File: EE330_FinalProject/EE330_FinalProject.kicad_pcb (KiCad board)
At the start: 2 copper layers, 20 parts, among them IC1 LT1490AIS8#PBF, J1 01x04_Pin, Q1 2N3904, Q2 2N3904, Q3 2N3904, Q4 2N3904

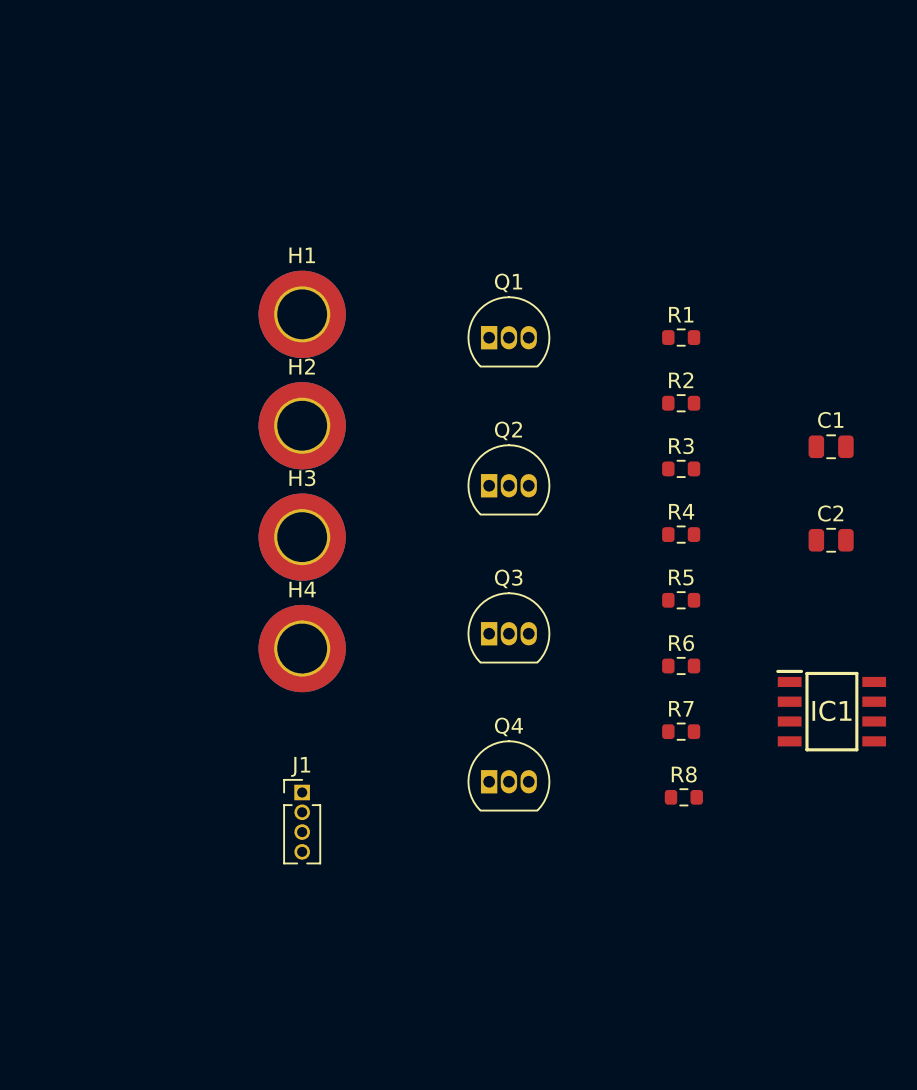
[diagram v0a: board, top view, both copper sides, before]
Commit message: Updated schematic and PCB based on the testing done today. Need to confirm physical setup before finalizing
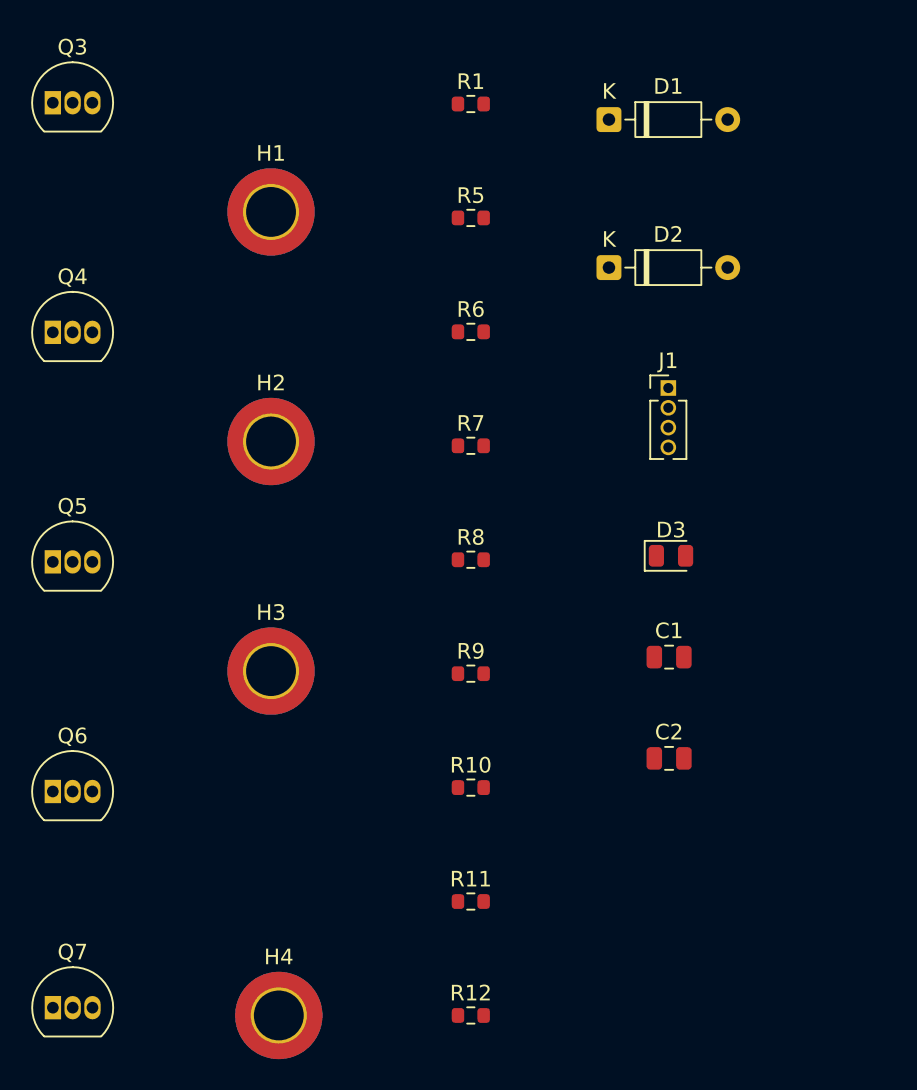
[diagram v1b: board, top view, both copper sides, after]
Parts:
- removed IC1: LT1490AIS8#PBF, Circuit_Craft_Footprints:LT1490
- removed Q1, Q2: 2N3904, Package_TO_SOT_THT:TO-92_Inline
- removed R2, R3, R4: 10k, Resistor_SMD:R_0603_1608Metric
- added D1: 1N4148, Diode_THT:D_DO-35_SOD27_P7.62mm_Horizontal, F.Cu at (65.2, 33.5)
- added D2: 1N4148, Diode_THT:D_DO-35_SOD27_P7.62mm_Horizontal, F.Cu at (65.2, 43.0)
- added D3: RED_LED, LED_SMD:LED_0805_2012Metric, F.Cu at (69.2, 61.5)
- added Q5: 2N3906, Package_TO_SOT_THT:TO-92_Inline, F.Cu at (29.5, 61.9)
- added Q6: 2N3904, Package_TO_SOT_THT:TO-92_Inline, F.Cu at (29.5, 76.6)
- added Q7: 2N3904, Package_TO_SOT_THT:TO-92_Inline, F.Cu at (29.5, 90.5)
- added R10: 1M, Resistor_SMD:R_0603_1608Metric, F.Cu at (56.3, 76.4)
- added R11: 1M, Resistor_SMD:R_0603_1608Metric, F.Cu at (56.3, 83.7)
- added R12: 150, Resistor_SMD:R_0603_1608Metric, F.Cu at (56.3, 91.0)
- added R9: 100k, Resistor_SMD:R_0603_1608Metric, F.Cu at (56.3, 69.1)
- C1: value 40u4 -> 33u3
- C2: value 17u3 -> 10u
- R1: value 10k -> 100k
- R5, R7: value 4k7 -> 10k
- moved Q3 44.1 mm to (29.5, 32.4)
- moved Q4 40.2 mm to (29.5, 47.2)
- moved J1 35.0 mm to (69.0, 50.7)
- moved R5 28.0 mm to (56.3, 39.8)
- moved R6 25.3 mm to (56.3, 47.1)
- moved H4 23.6 mm to (44.0, 91.0)
- moved R7 22.8 mm to (56.3, 54.4)
- moved R8 20.5 mm to (56.3, 61.8)
- moved R1 20.2 mm to (56.3, 32.5)
- moved C2 17.4 mm to (69.0, 74.5)
- moved C1 17.0 mm to (69.0, 68.0)
- moved H3 8.83 mm to (43.5, 68.9)
- moved H1 6.87 mm to (43.5, 39.4)
- moved H2 2.24 mm to (43.5, 54.2)
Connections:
- R1 pad 1: Battery -> Net-(D3-A)
- R1 pad 2: Oscillator_NOT -> GND

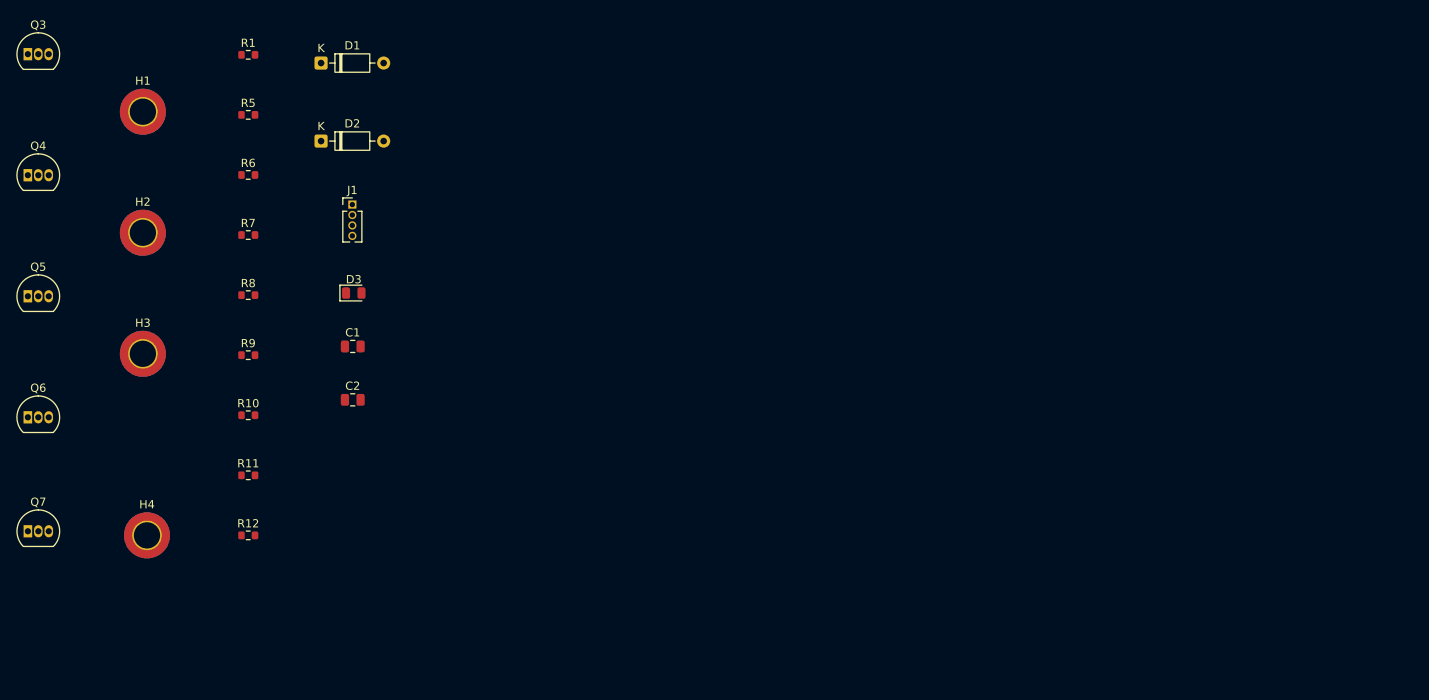
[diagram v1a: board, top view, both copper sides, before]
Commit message: Finished PCB Design with layout and routing
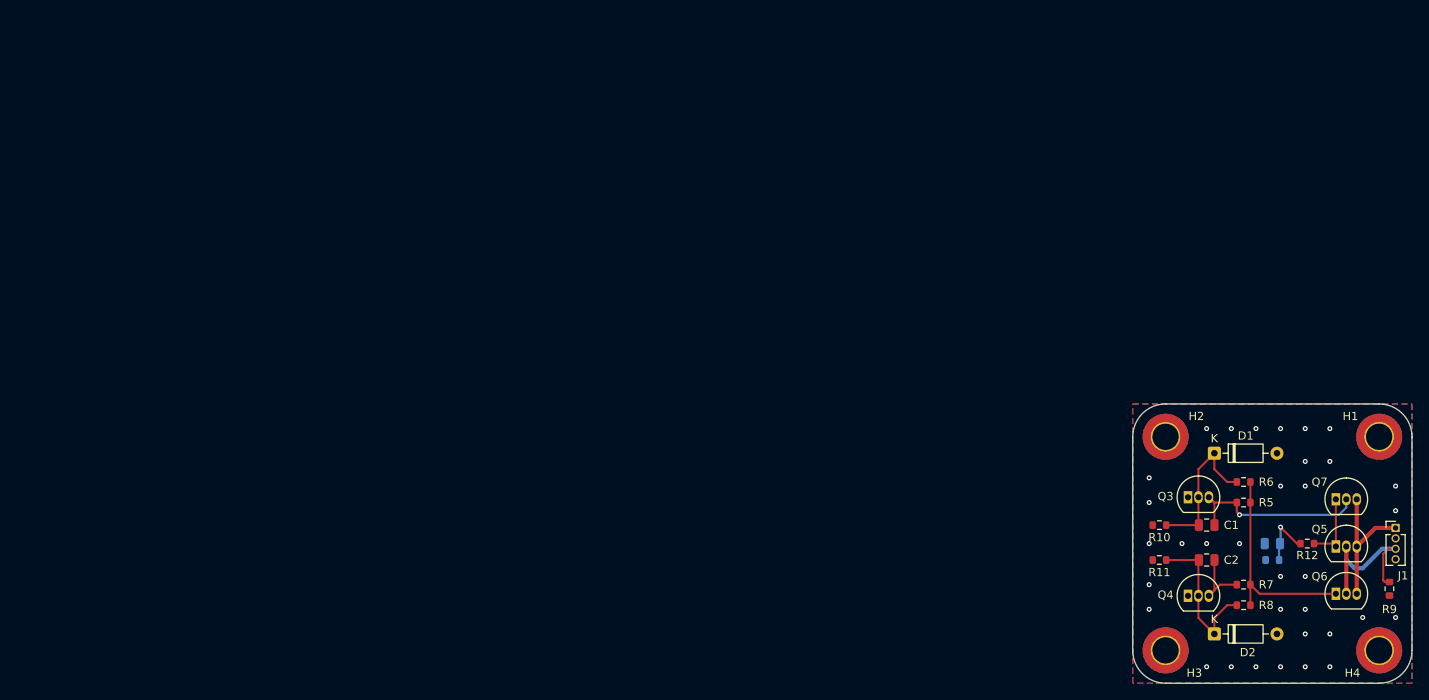
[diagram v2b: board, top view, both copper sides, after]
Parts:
- D3, R1: moved to B.Cu
- moved Q5 162.1 mm to (188.7, 92.4)
- moved Q6 160.7 mm to (188.7, 98.1)
- moved Q7 159.3 mm to (188.7, 86.6)
- moved H1 155.6 mm to (194.0, 79.0)
- moved Q3 151.2 mm to (170.7, 86.4)
- moved H4 150.7 mm to (194.0, 105.0)
- moved Q4 150.2 mm to (170.7, 98.4)
- moved R9 141.8 mm to (195.2, 97.5), turned to -90 degrees
- moved R1 139.0 mm to (181.0, 94.0), turned to 180 degrees
- moved J1 133.0 mm to (196.0, 90.1)
- moved R5 130.0 mm to (177.5, 87.0), turned to 180 degrees
- moved H3 129.6 mm to (168.0, 105.0)
- moved R12 128.9 mm to (185.2, 92.0), turned to 180 degrees
- moved R7 128.4 mm to (177.5, 97.0), turned to 180 degrees
- moved H2 127.0 mm to (168.0, 79.0)
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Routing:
- net Oscillator: track 0.00 -> 25.9 mm
- net LED_OUT: track 0.00 -> 23.3 mm, vias 0 -> 1
- net SolarPanel: track 0.00 -> 20.6 mm
- net /N2: track 0.00 -> 19.1 mm
- net /N1: track 0.00 -> 18.9 mm
- net Battery: track 0.00 -> 17.2 mm
- net Net-(Q4-C): track 0.00 -> 8.61 mm
- net Oscillator_NOT: track 0.00 -> 8.55 mm
- net Net-(D3-A): track 0.00 -> 7.33 mm, vias 0 -> 1
- net GND: vias 0 -> 34
- added copper zone on B.Cu, net GND
- added copper zone on F.Cu, net GND
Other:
- board outline added: 34 x 34 mm
- board text added: "BATT"
- board text added: "EE330"
- board text added: "EMERGENCY INDICATOR"
- board text added: "GND"
- board text added: "K"
- board text added: "SP"
